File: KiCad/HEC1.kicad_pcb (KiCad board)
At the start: 2 copper layers, 243.8 x 170.2 mm, 654 parts, among them J1 Barrel_Jack_Switch, J2 Conn_02x12_Odd_Even, J3 Conn_02x05_Odd_Even, J5 Screw_Terminal_01x02, J6 DE9_Plug_MountingHoles, J7 AudioJack3, J8 NES_Port_Male, J9 Conn_02x14_Odd_Even, SW1 SW_DIP_x04, SW2 SW_Push, U1 Z80CPU, U10 74LS32, U11 74LS00, U12 74LS04, U13 74LS245, U14 74LS245, U15 74LS32, U16 74LS32, U17 74LS20, U18 74LS138, U19 74LS30, U2 AS6C4008-55PCN, U20 74LS574, U21 74LS574, U22 74LS02, U23 74LS74, U24 74LS74, U25 74LS541, U26 74LS541, U27 74LS74, U28 74LS30, U29 74LS74, U3 AS6C4008-55PCN, U30 74LS74, U31 74LS32, U32 LM79M05_TO220, U33 74LS20, U34 74LS393, U35 74LS08, U36 74LS574, U37 74LS32, U38 74LS47, U39 74LS47, U4 CY7C199, U40 DA04-11EWA, U41 74LS02, U42 74LS06, U44 74LS541, U5 CY7C199, U6 74LS138, U7 28C256, U8 74LS138, U9 74LS574, X1 CXO_DIP8, Y1 Crystal

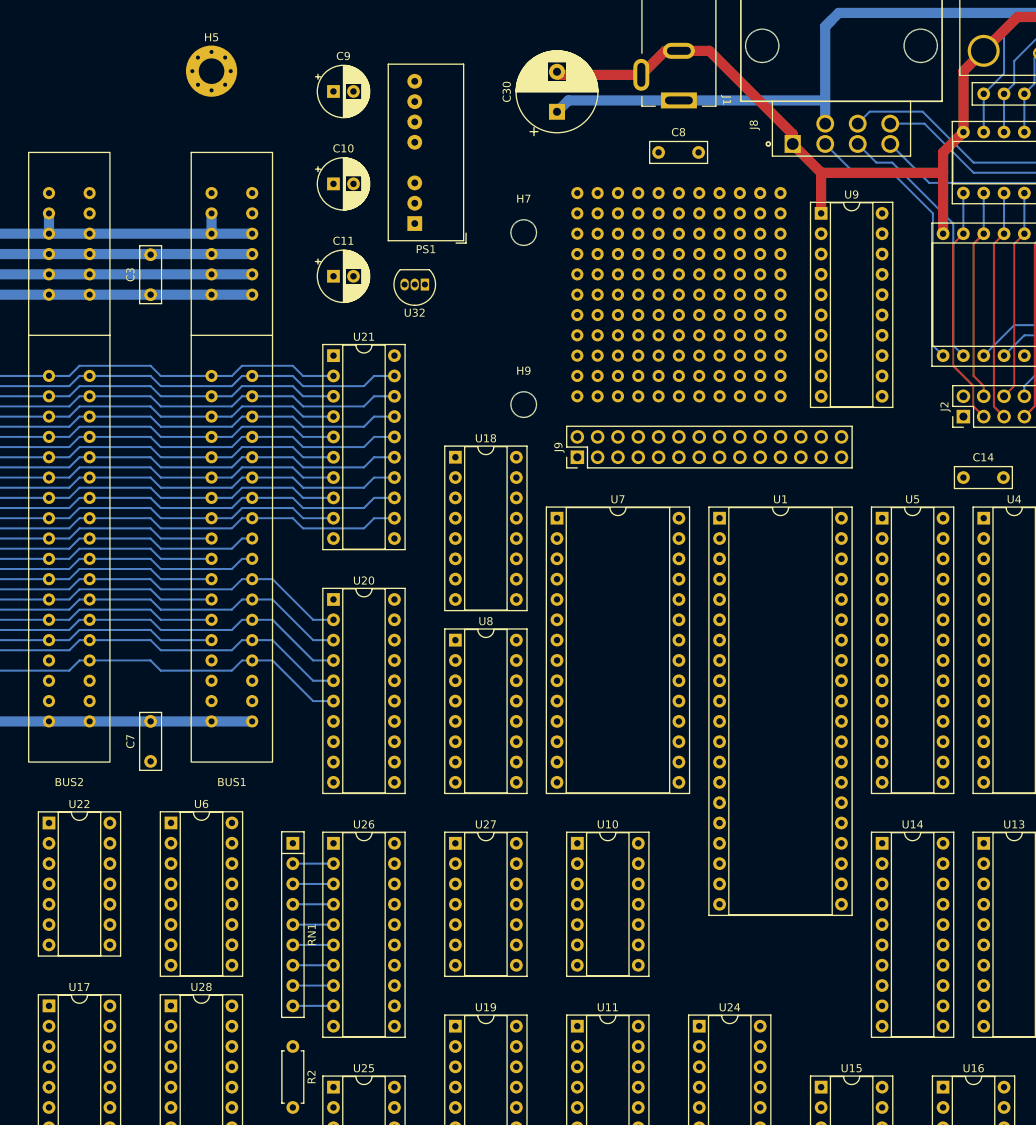
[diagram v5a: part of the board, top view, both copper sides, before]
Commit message: More routing
Swapped U15 and U16, minor adjustments to schematic. routing of power lines.
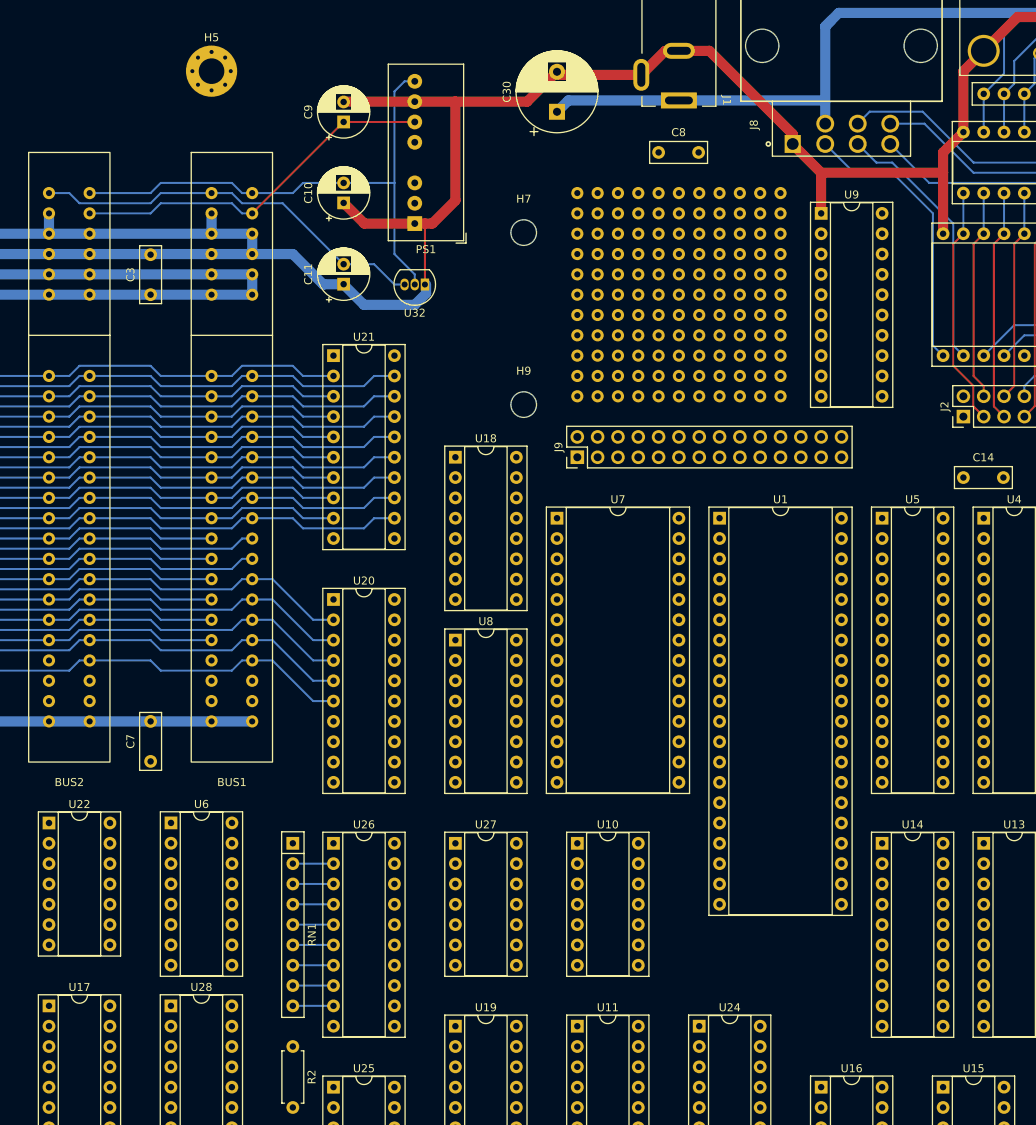
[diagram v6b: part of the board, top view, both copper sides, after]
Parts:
- moved U15 15.2 mm to (205.7, 162.6)
- moved U16 15.2 mm to (190.5, 162.6)
- moved C9 4.02 mm to (130.8, 41.9), turned to 90 degrees
- moved C10 2.70 mm to (130.8, 52.0), turned to 90 degrees
- moved C11 1.61 mm to (130.8, 62.2), turned to 90 degrees
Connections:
- U16 pad 1: /HEC_CPU/~{WR} -> /HEC_CPU/~{IOPORT_H}
- U16 pad 10: /HEC_CPU/~{RD} -> /HEC_Memory/~{PAGE_H}
- U16 pad 11: Net-(U21-OE) -> /HEC_Memory/~{PAGE_L_WE}
- U16 pad 12: /HEC_CPU/~{IOPORT_H} -> /HEC_CPU/~{WR}
- U16 pad 13: /HEC_CPU/~{RD} -> /HEC_Memory/~{PAGE_L}
- U16 pad 2: /HEC_Memory/~{PAGE_L} -> /HEC_CPU/~{RD}
- U16 pad 3: /HEC_Memory/~{PAGE_L_WE} -> Net-(U21-OE)
- U16 pad 4: /HEC_CPU/~{WR} -> /HEC_CPU/~{IOPORT_L}
- U16 pad 5: /HEC_Memory/~{PAGE_H} -> /HEC_CPU/~{RD}
- U16 pad 6: /HEC_Memory/~{PAGE_H_WE} -> Net-(U20-OE)
- U16 pad 8: Net-(U20-OE) -> /HEC_Memory/~{PAGE_H_WE}
- U16 pad 9: /HEC_CPU/~{IOPORT_L} -> /HEC_CPU/~{WR}
- U37 pad 10: /HEC_CPU/~{MREQ} -> L
- U37 pad 11: unconnected-(U37-Pad11) -> /HEC_Memory/~{RAM_OE}
- U37 pad 12: L -> Net-(U30A-Q)
- U37 pad 13: L -> /HEC_CPU/~{RD}
- U37 pad 4: Net-(U30A-Q) -> /HEC_CPU/~{RFSH}
- U37 pad 5: /HEC_CPU/~{RD} -> /HEC_CPU/~{MREQ}
- U37 pad 6: /HEC_Memory/~{RAM_OE} -> Net-(U36-Cp)
- U37 pad 8: Net-(U36-Cp) -> unconnected-(U37-Pad8)
- U37 pad 9: /HEC_CPU/~{RFSH} -> L
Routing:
- net L: track 423.1 -> 516.2 mm
- net /HEC_IO/-12V: track 0.00 -> 67.9 mm
- net /HEC_IO/-5V: track 0.00 -> 50.2 mm
- net /HEC_IO/+12V: track 0.00 -> 46.4 mm
- net H: track 303.2 -> 305.7 mm

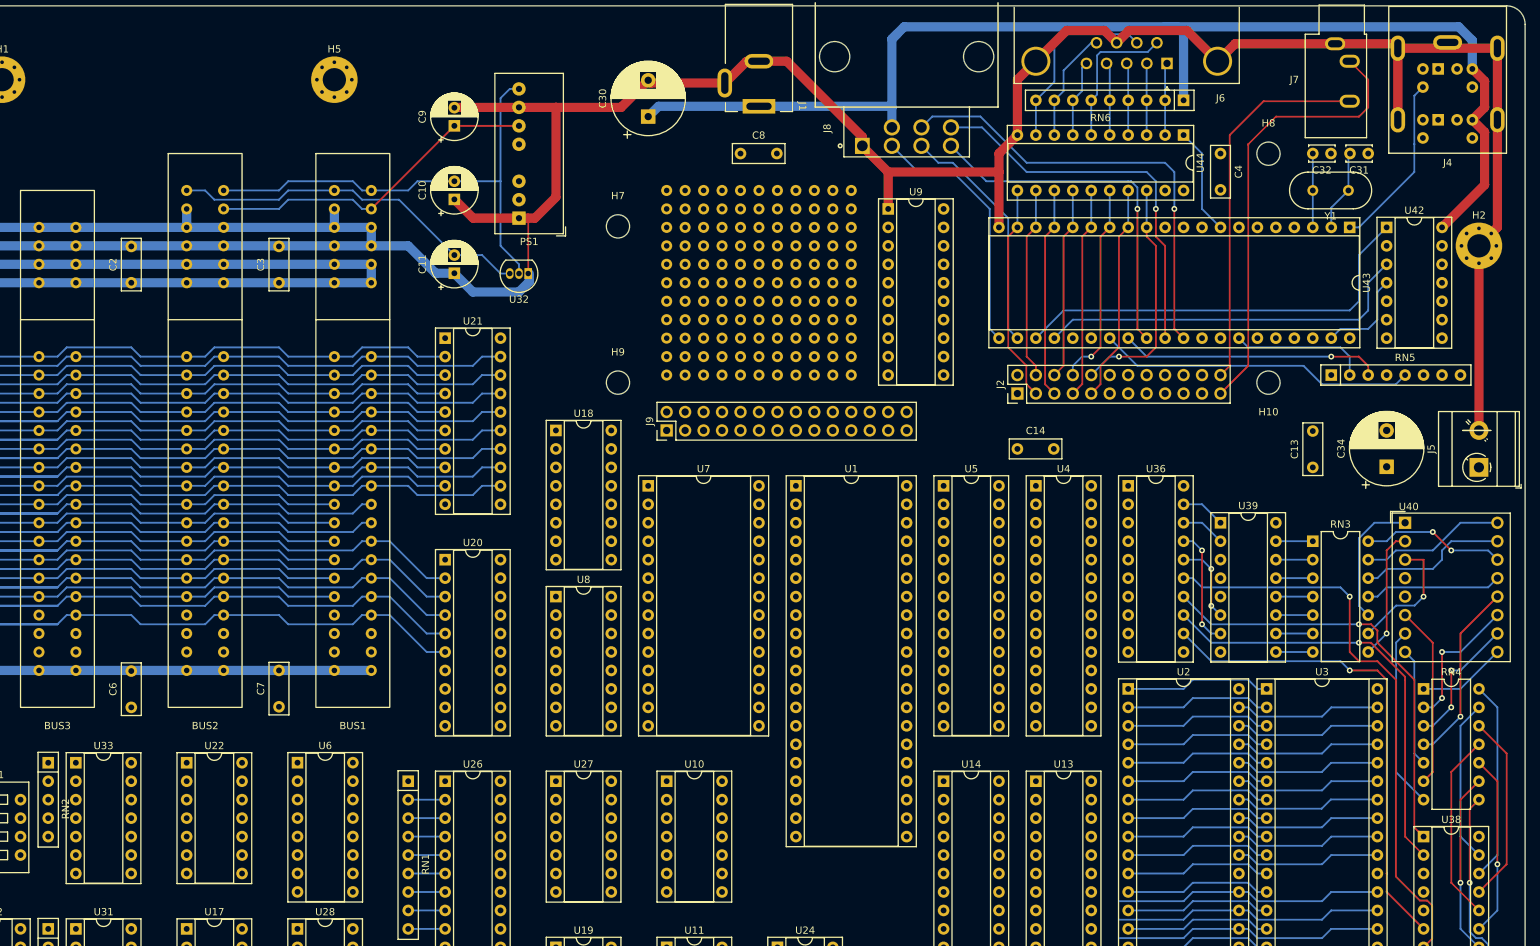
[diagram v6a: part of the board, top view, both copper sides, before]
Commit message: More routing
Finished routing the IO part of the board. Currently it doesn't seem like a 4-layer board is needed.
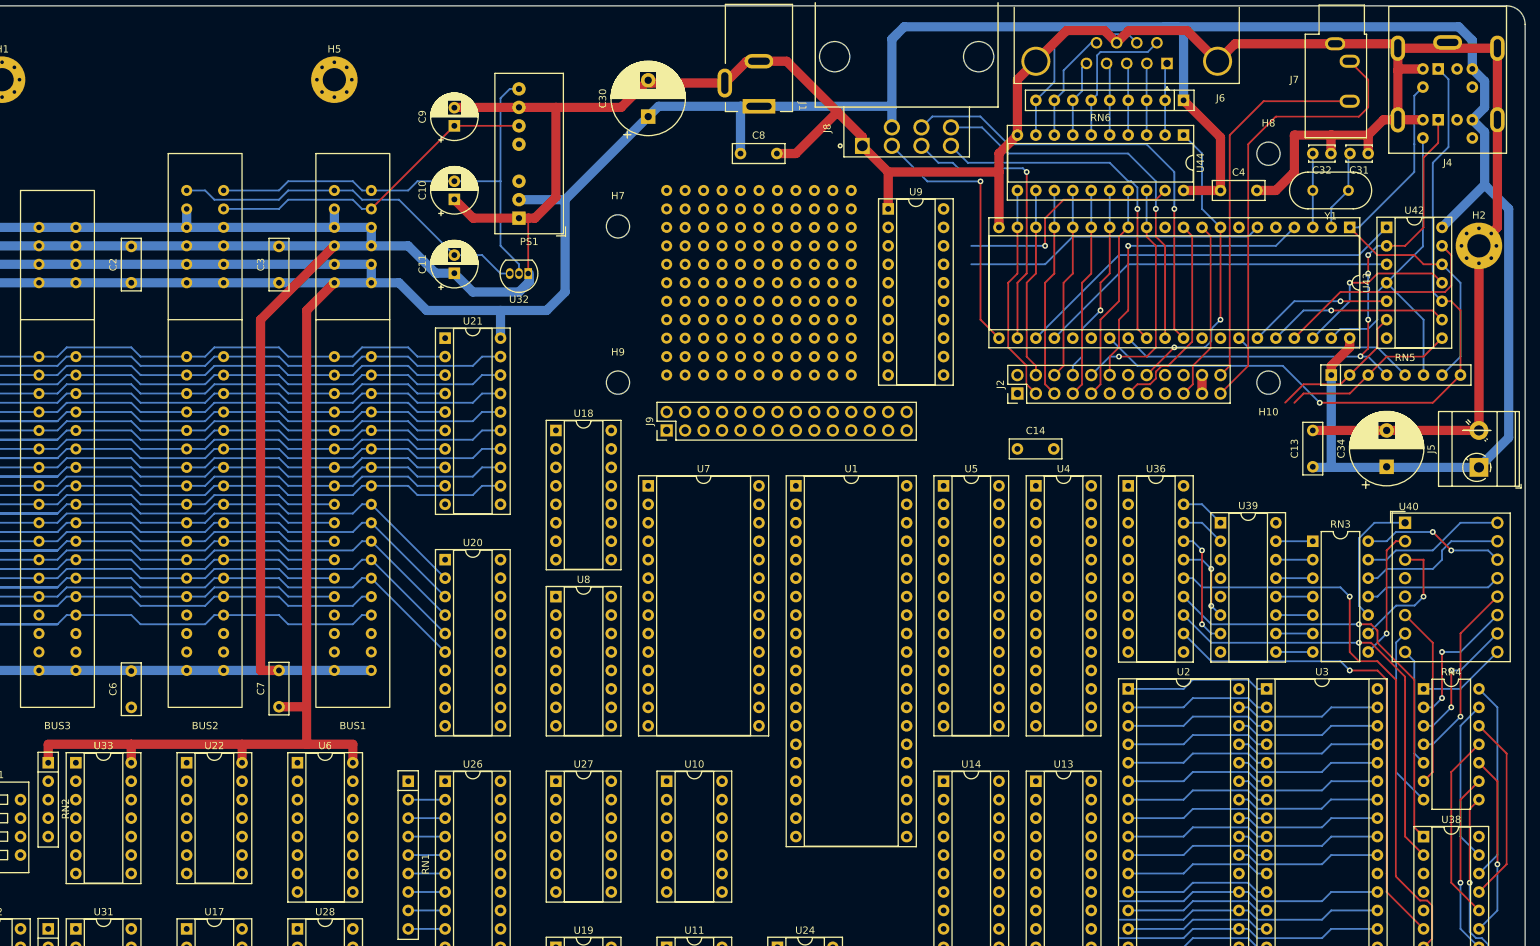
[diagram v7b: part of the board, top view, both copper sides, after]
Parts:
- moved C4 5.08 mm to (236.2, 50.8), turned to 0 degrees
- moved C13 0.08 mm to (248.9, 88.8)
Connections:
- BUS1 pad 18: /HEC_IO/~{IOR} -> /HEC_IO/A0
- BUS1 pad 20: /HEC_CPU/~{WR} -> /HEC_IO/A1
- BUS1 pad 22: /HEC_IO/A0 -> /HEC_IO/A2
- BUS1 pad 24: /HEC_IO/A1 -> /HEC_IO/A3
- BUS1 pad 26: /HEC_IO/A2 -> /HEC_IO/A4
- BUS1 pad 28: /HEC_IO/A3 -> /HEC_IO/~{IOR}
- BUS1 pad 30: /HEC_IO/A4 -> /HEC_CPU/~{WR}
- BUS2 pad 18: /HEC_IO/~{IOR} -> /HEC_IO/A0
- BUS2 pad 20: /HEC_CPU/~{WR} -> /HEC_IO/A1
- BUS2 pad 22: /HEC_IO/A0 -> /HEC_IO/A2
- BUS2 pad 24: /HEC_IO/A1 -> /HEC_IO/A3
- BUS2 pad 26: /HEC_IO/A2 -> /HEC_IO/A4
- BUS2 pad 28: /HEC_IO/A3 -> /HEC_IO/~{IOR}
- BUS2 pad 30: /HEC_IO/A4 -> /HEC_CPU/~{WR}
- BUS3 pad 18: /HEC_IO/~{IOR} -> /HEC_IO/A0
- BUS3 pad 20: /HEC_CPU/~{WR} -> /HEC_IO/A1
- BUS3 pad 22: /HEC_IO/A0 -> /HEC_IO/A2
- BUS3 pad 24: /HEC_IO/A1 -> /HEC_IO/A3
- BUS3 pad 26: /HEC_IO/A2 -> /HEC_IO/A4
- BUS3 pad 28: /HEC_IO/A3 -> /HEC_IO/~{IOR}
- BUS3 pad 30: /HEC_IO/A4 -> /HEC_CPU/~{WR}
- BUS4 pad 18: /HEC_IO/~{IOR} -> /HEC_IO/A0
- BUS4 pad 20: /HEC_CPU/~{WR} -> /HEC_IO/A1
- BUS4 pad 22: /HEC_IO/A0 -> /HEC_IO/A2
- BUS4 pad 24: /HEC_IO/A1 -> /HEC_IO/A3
- BUS4 pad 26: /HEC_IO/A2 -> /HEC_IO/A4
- BUS4 pad 28: /HEC_IO/A3 -> /HEC_IO/~{IOR}
- BUS4 pad 30: /HEC_IO/A4 -> /HEC_CPU/~{WR}
- J4 pad A1: Net-(RN5-R4) -> Net-(RN5-R7)
- J4 pad A5: Net-(RN5-R5) -> Net-(RN5-R6)
- J4 pad B1: Net-(RN5-R2) -> Net-(RN5-R3)
- J4 pad B5: Net-(RN5-R3) -> Net-(RN5-R5)
- RN5 pad 2: Net-(RN5-R1) -> /HEC_Peripherals/~{KB_IRQ}
- RN5 pad 3: Net-(RN5-R2) -> /HEC_Peripherals/~{MS_IRQ}
- RN5 pad 7: /HEC_Peripherals/~{MS_IRQ} -> Net-(RN5-R6)
- RN5 pad 8: /HEC_Peripherals/~{KB_IRQ} -> Net-(RN5-R7)
- U42 pad 10: Net-(RN5-R4) -> Net-(RN5-R7)
- U42 pad 12: Net-(RN5-R5) -> Net-(RN5-R6)
- U42 pad 2: Net-(RN5-R2) -> Net-(RN5-R3)
- U42 pad 4: Net-(RN5-R3) -> Net-(RN5-R5)
- U43 pad 1: Net-(RN5-R5) -> Net-(RN5-R6)
- U43 pad 27: Net-(RN5-R4) -> Net-(RN5-R7)
- U43 pad 28: Net-(RN5-R2) -> Net-(RN5-R3)
- U43 pad 34: Net-(RN5-R1) -> Net-(RN5-R4)
- U43 pad 39: Net-(RN5-R3) -> Net-(RN5-R5)
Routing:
- net H: track 305.7 -> 604.8 mm
- net L: track 516.2 -> 656.0 mm
- net Net-(RN5-R7): track 0.00 -> 99.4 mm, vias 0 -> 1
- net Net-(RN5-R3): track 13.0 -> 76.9 mm, vias 0 -> 4
- net Net-(RN5-R6): track 0.00 -> 56.4 mm
- net /HEC_IO/A0: track 133.1 -> 178.4 mm
- net /HEC_Peripherals/~{RESET}: track 0.00 -> 42.7 mm, vias 0 -> 1
- net /HEC_IO/~{IO_CS2}: track 0.00 -> 41.5 mm
- net Net-(RN5-R2): track 35.9 -> 0.00 mm, vias 1 -> 0
- net /HEC_IO/~{IO_CS3}: track 0.00 -> 32.1 mm, vias 0 -> 1
- net Net-(U43-KBCO): track 0.00 -> 30.6 mm
- net /HEC_CPU/~{RD}: track 14.8 -> 41.8 mm, vias 0 -> 2
- net Net-(RN5-R5): track 24.2 -> 49.8 mm
- net Net-(U43-MS_OBFO): track 0.00 -> 25.0 mm, vias 0 -> 1
- net /HEC_Peripherals/~{MS_IRQ}: track 0.00 -> 24.0 mm
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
